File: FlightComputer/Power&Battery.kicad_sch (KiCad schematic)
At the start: 0 parts

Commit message: Adding 3.3V regulator, usb c connector, battery connector and calculations sheet
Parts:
- added C1, C4, C6: 100n, Capacitor_SMD:C_0603_1608Metric_Pad1.08x0.95mm_HandSolder, symbol Device:C_Small
- added C2, C3: 22uF, Capacitor_SMD:C_0603_1608Metric_Pad1.08x0.95mm_HandSolder, symbol Device:C_Small
- added C5: 10u, Capacitor_SMD:C_0603_1608Metric_Pad1.08x0.95mm_HandSolder, symbol Device:C_Small
- added C7: 10n, Capacitor_SMD:C_0603_1608Metric_Pad1.08x0.95mm_HandSolder, symbol Device:C_Small
- added D1: UPDATE, symbol Device:D_TVS_Small
- added D2: RED, symbol Device:LED_Small
- added D3: ORANGE, symbol Device:LED_Small
- added L1: 4.7u, symbol Device:L_Small
- added R10, R11: 1k, Resistor_SMD:R_0603_1608Metric_Pad0.98x0.95mm_HandSolder, symbol Device:R_Small
- added R4: 110k, Resistor_SMD:R_0603_1608Metric_Pad0.98x0.95mm_HandSolder, symbol Device:R_Small
- added R5: 11k, Resistor_SMD:R_0603_1608Metric_Pad0.98x0.95mm_HandSolder, symbol Device:R_Small
- added R6: 135k, Resistor_SMD:R_0603_1608Metric_Pad0.98x0.95mm_HandSolder, symbol Device:R_Small
- added R7: 30k, Resistor_SMD:R_0603_1608Metric_Pad0.98x0.95mm_HandSolder, symbol Device:R_Small
- added R8: 24k, Resistor_SMD:R_0603_1608Metric_Pad0.98x0.95mm_HandSolder, symbol Device:R_Small
- added R9: 5.1k, Resistor_SMD:R_0603_1608Metric_Pad0.98x0.95mm_HandSolder, symbol Device:R_Small
- added U1: TPS562202, Package_TO_SOT_SMD:SOT-563, symbol Regulator_Switching:TPS562202
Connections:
- new net: D2.2 (A), R10.2
- new net: D3.2 (A), R11.2
- new net +3V3: C2.1, C3.1, L1.2, R6.1
- new net 3V3: R11.1
- new net EN: R4.2, R5.1, U1.5 (EN)
- new net GND: C1.2, C2.2, C3.2, C5.2, C6.2, C7.2, D1.1 (A1), D2.1 (K), D3.1 (K), R5.2, R7.2, R9.2, U1.3 (GND)
- new net VBATT: C1.1, C5.1, C6.1, D1.2 (A2), R10.1, R4.1, R8.1, U1.1 (VIN)
- new net VBST: C4.1, U1.4 (VBST)
- new net VFB: R6.2, R7.1, U1.6 (VFB)
- new net VSW: C4.2, L1.1, U1.2 (SW)
- new net aIN_VBAT: C7.1, R8.2, R9.1
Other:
- note added: "3V3 Switch Regulator"
- note added: "Indicator LEDs"
- note added: "VBAT Monitor"

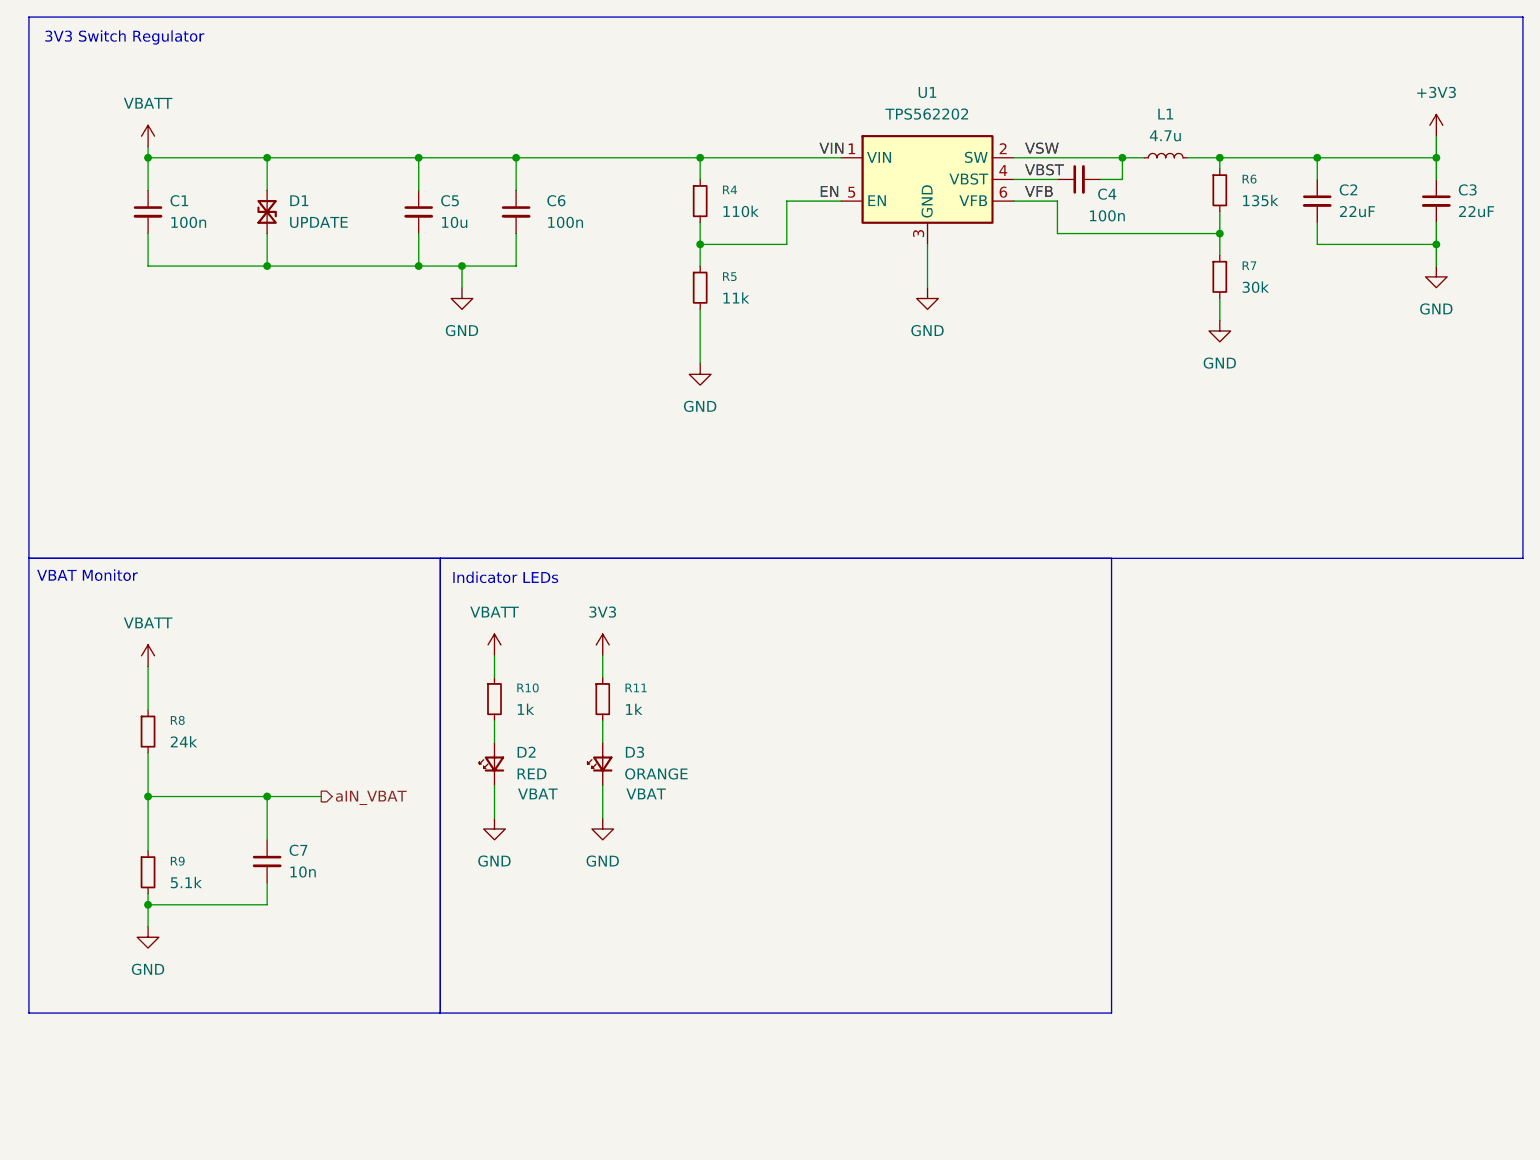
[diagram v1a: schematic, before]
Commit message: Updating calculations, sensors page and adding micro page
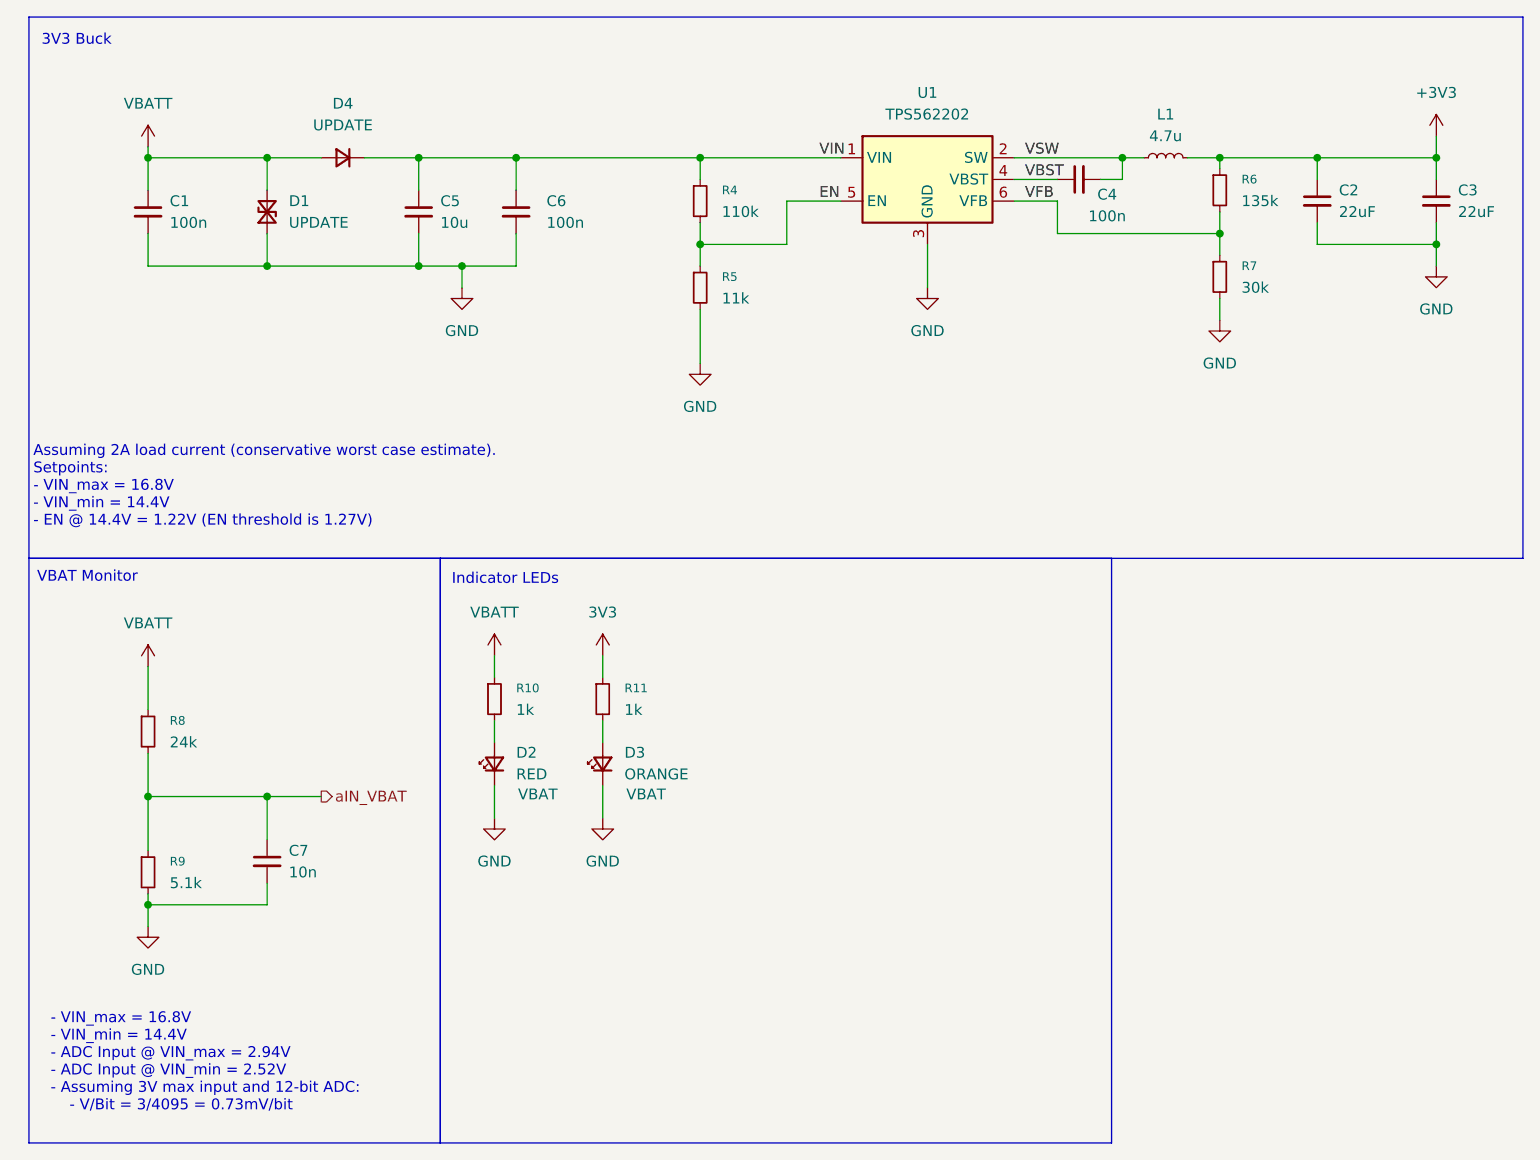
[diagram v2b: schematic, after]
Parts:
- added D4: UPDATE, symbol Device:D_Small
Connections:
- net VBATT: now also D4.2 (A); no longer C5.1, C6.1, R4.1, U1.1 (VIN)
- new net VIN: C5.1, C6.1, D4.1 (K), R4.1, U1.1 (VIN)
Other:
- note added: "- VIN_max = 16.8V - VIN_min = 14.4V - ADC Input @ VIN_max = 2.94V - ADC Input @ VIN_min = 2.52V - Assuming 3V max input and 12-bit ADC: - V/Bit = 3/4095 = 0.73mV/bit"
- note added: "3V3 Buck"
- note added: "Assuming 2A load current (conservative worst case estimate). Setpoints: - VIN_max = 16.8V - VIN_min = 14.4V - EN @ 14.4V = 1.22V (EN threshold is 1.27V)"
- note removed: "3V3 Switch Regulator"
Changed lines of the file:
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@@
 	(rectangle
 		(start 60.96 76.2)
-		(end 139.7 129.54)
+		(end 139.7 144.78)
 		(stroke
 			(width 0)
@@
 	(rectangle
 		(start 12.7 76.2)
-		(end 60.96 129.54)
+		(end 60.96 144.78)
 		(stroke
 			(width 0)
@@
 		)
 	)
-	(text "3V3 Switch Regulator\n"
+	(text "3V3 Buck\n"
 		(exclude_from_sim no)
-		(at 23.876 15.24 0)
+		(at 18.288 15.494 0)
 		(effects
 			(font
@@
 		)
 	)
+	(text "- VIN_max = 16.8V\n- VIN_min = 14.4V\n- ADC Input @ VIN_max = 2.94V\n- ADC Input @ VIN_min = 2.52V\n- Assuming 3V max input and 12-bit ADC:\n	- V/Bit = 3/4095 = 0.73mV/bit\n"
+		(exclude_from_sim no)
+		(at 15.24 135.382 0)
+		(effects
+			(font
+				(size 1.27 1.27)
+			)
+			(justify left)
+		)
+	)
+	(text "Assuming 2A load current (conservative worst case estimate).\nSetpoints:\n- VIN_max = 16.8V\n- VIN_min = 14.4V\n- EN @ 14.4V = 1.22V (EN threshold is 1.27V)\n"
+		(exclude_from_sim no)
+		(at 13.208 67.818 0)
+		(effects
+			(font
+				(size 1.27 1.27)
+			)
+			(justify left)
+		)
+	)
 	(text "VBAT Monitor\n"
 		(exclude_from_sim no)
@@
 	(wire
 		(pts
+			(xy 52.07 29.21) (xy 58.42 29.21)
+		)
+		(stroke
+			(width 0)
+			(type default)
+		)
+	)
+	(wire
+		(pts
 			(xy 67.31 102.87) (xy 67.31 106.68)
 		)
@@
 	(wire
 		(pts
-			(xy 40.64 29.21) (xy 58.42 29.21)
+			(xy 40.64 29.21) (xy 46.99 29.21)
 		)
 		(stroke
@@
 					(unit 1)
 				)
+			)
+		)
+	)
+	(symbol
+		(lib_id "Device:D_Small")
+		(at 49.53 29.21 180)
+		(unit 1)
+		(exclude_from_sim no)
+		(in_bom yes)
+		(on_board yes)
+		(dnp no)
+		(fields_autoplaced yes)
+		(property "Reference" "D4"
+			(at 49.53 22.86 0)
+			(effects
+				(font
+					(size 1.27 1.27)
+				)
+			)
+		)
+		(property "Value" "UPDATE"
+			(at 49.53 25.4 0)
+			(effects
+				(font
+					(size 1.27 1.27)
+				)
+			)
+		)
+		(property "Footprint" ""
+			(at 49.53 29.21 90)
+			(effects
+				(font
+					(size 1.27 1.27)
+				)
+				(hide yes)
+			)
+		)
+		(property "Datasheet" "~"
+			(at 49.53 29.21 90)
+			(effects
+				(font
+					(size 1.27 1.27)
+				)
+				(hide yes)
+			)
+		)
+		(property "Description" "Diode, small symbol"
+			(at 49.53 29.21 0)
+			(effects
+				(font
+					(size 1.27 1.27)
+				)
+				(hide yes)
+			)
+		)
+		(property "Sim.Device" "D"
+			(at 49.53 29.21 0)
+			(effects
+				(font
+					(size 1.27 1.27)
+				)
+				(hide yes)
+			)
+		)
+		(property "Sim.Pins" "1=K 2=A"
+			(at 49.53 29.21 0)
+			(effects
+				(font
+					(size 1.27 1.27)
+				)
+				(hide yes)
+			)
+		)
+		(pin "1"
+		)
+		(pin "2"
+		)
+		(instances
+			(project ""
+				(path "/e49ed6f8-44fe-4a80-bc0f-4dd2a2b50b4e/f82fc492-cd97-4243-936e-52c3020bdf96"
+					(reference "D4")
+					(unit 1)
+				)

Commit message: Various updates
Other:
- company: (none) -> MD
- title: (none) -> Flight Computer: Power & Battery
- moved on the sheet: C7
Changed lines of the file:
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@@
 	(generator_version "9.0")
 	(paper "A4")
+	(title_block
+		(title "Flight Computer: Power & Battery")
+		(date "2026-01-19")
+		(rev "A0.1")
+		(company "MD")
+	)
 	(rectangle
 		(start 12.7 12.7)
@@
 	)
 	(junction
+		(at 35.56 104.14)
+		(diameter 0)
+		(color 0 0 0 0)
+	)
+	(junction
 		(at 26.67 116.84)
 		(diameter 0)
@@
 	)
 	(junction
-		(at 40.64 104.14)
+		(at 168.91 29.21)
 		(diameter 0)
 		(color 0 0 0 0)
@@
 	(wire
 		(pts
-			(xy 40.64 116.84) (xy 26.67 116.84)
+			(xy 35.56 116.84) (xy 26.67 116.84)
 		)
 		(stroke
@@
 	(wire
 		(pts
-			(xy 40.64 104.14) (xy 26.67 104.14)
+			(xy 35.56 104.14) (xy 46.99 104.14)
 		)
 		(stroke
@@
 	(wire
 		(pts
+			(xy 35.56 104.14) (xy 26.67 104.14)
+		)
+		(stroke
+			(width 0)
+			(type default)
+		)
+	)
+	(wire
+		(pts
 			(xy 67.31 87.63) (xy 67.31 90.17)
 		)
@@
 	(wire
 		(pts
-			(xy 40.64 114.3) (xy 40.64 116.84)
+			(xy 35.56 113.03) (xy 35.56 116.84)
 		)
 		(stroke
@@
 	(wire
 		(pts
-			(xy 40.64 104.14) (xy 46.99 104.14)
-		)
-		(stroke
-			(width 0)
-			(type default)
-		)
-	)
-	(wire
-		(pts
-			(xy 177.8 29.21) (xy 163.83 29.21)
+			(xy 177.8 29.21) (xy 168.91 29.21)
 		)
 		(stroke
@@
 	(wire
 		(pts
-			(xy 40.64 109.22) (xy 40.64 104.14)
+			(xy 35.56 107.95) (xy 35.56 104.14)
 		)
 		(stroke
@@
 		(pts
 			(xy 40.64 29.21) (xy 26.67 29.21)
+		)
+		(stroke
+			(width 0)
+			(type default)
+		)
+	)
+	(wire
+		(pts
+			(xy 168.91 29.21) (xy 163.83 29.21)
 		)
 		(stroke
@@
 	(symbol
 		(lib_id "Device:C_Small")
-		(at 40.64 111.76 0)
+		(at 35.56 110.49 0)
 		(unit 1)
 		(exclude_from_sim no)
@@
 		(fields_autoplaced yes)
 		(property "Reference" "C7"
-			(at 43.18 110.4962 0)
+			(at 38.1 109.2262 0)
 			(effects
 				(font
@@
 		)
 		(property "Value" "10n"
-			(at 43.18 113.0362 0)
+			(at 38.1 111.7662 0)
 			(effects
 				(font
@@
 		)
 		(property "Footprint" "Capacitor_SMD:C_0603_1608Metric_Pad1.08x0.95mm_HandSolder"
-			(at 40.64 111.76 0)
+			(at 35.56 110.49 0)
 			(effects
 				(font
@@
 		)
 		(property "Datasheet" "~"
-			(at 40.64 111.76 0)
+			(at 35.56 110.49 0)
 			(effects
 				(font
@@
 		)
 		(property "Description" "Unpolarized capacitor, small symbol"
-			(at 40.64 111.76 0)
+			(at 35.56 110.49 0)
 			(effects
 				(font
@@
 					(unit 1)
 				)
+			)
+		)
+	)
+	(symbol
+		(lib_id "power:PWR_FLAG")
+		(at 168.91 29.21 0)
+		(unit 1)
+		(exclude_from_sim no)
+		(in_bom yes)
+		(on_board yes)
+		(dnp no)
+		(fields_autoplaced yes)
+		(property "Reference" "#FLG03"
+			(at 168.91 27.305 0)
+			(effects
+				(font
+					(size 1.27 1.27)
+				)
+				(hide yes)
+			)
+		)
+		(property "Value" "PWR_FLAG"
+			(at 168.91 24.13 0)
+			(effects
+				(font
+					(size 1.27 1.27)
+				)
+			)
+		)
+		(property "Footprint" ""
+			(at 168.91 29.21 0)
+			(effects
+				(font
+					(size 1.27 1.27)
+				)
+				(hide yes)
+			)
+		)
+		(property "Datasheet" "~"
+			(at 168.91 29.21 0)
+			(effects
+				(font
+					(size 1.27 1.27)
+				)
+				(hide yes)
+			)
+		)
+		(property "Description" "Special symbol for telling ERC where power comes from"
+			(at 168.91 29.21 0)
+			(effects
+				(font
+					(size 1.27 1.27)
+				)
+				(hide yes)
+			)
+		)
+		(pin "1"
+		)
+		(instances
+			(project "FlightComputer"
+				(path "/e49ed6f8-44fe-4a80-bc0f-4dd2a2b50b4e/f82fc492-cd97-4243-936e-52c3020bdf96"
+					(reference "#FLG03")
+					(unit 1)
+				)
